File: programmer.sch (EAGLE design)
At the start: 25 parts, among them IC2 74241, U1 ATMEGA8U2, X2 USB-MICROB, Y1 16MHz

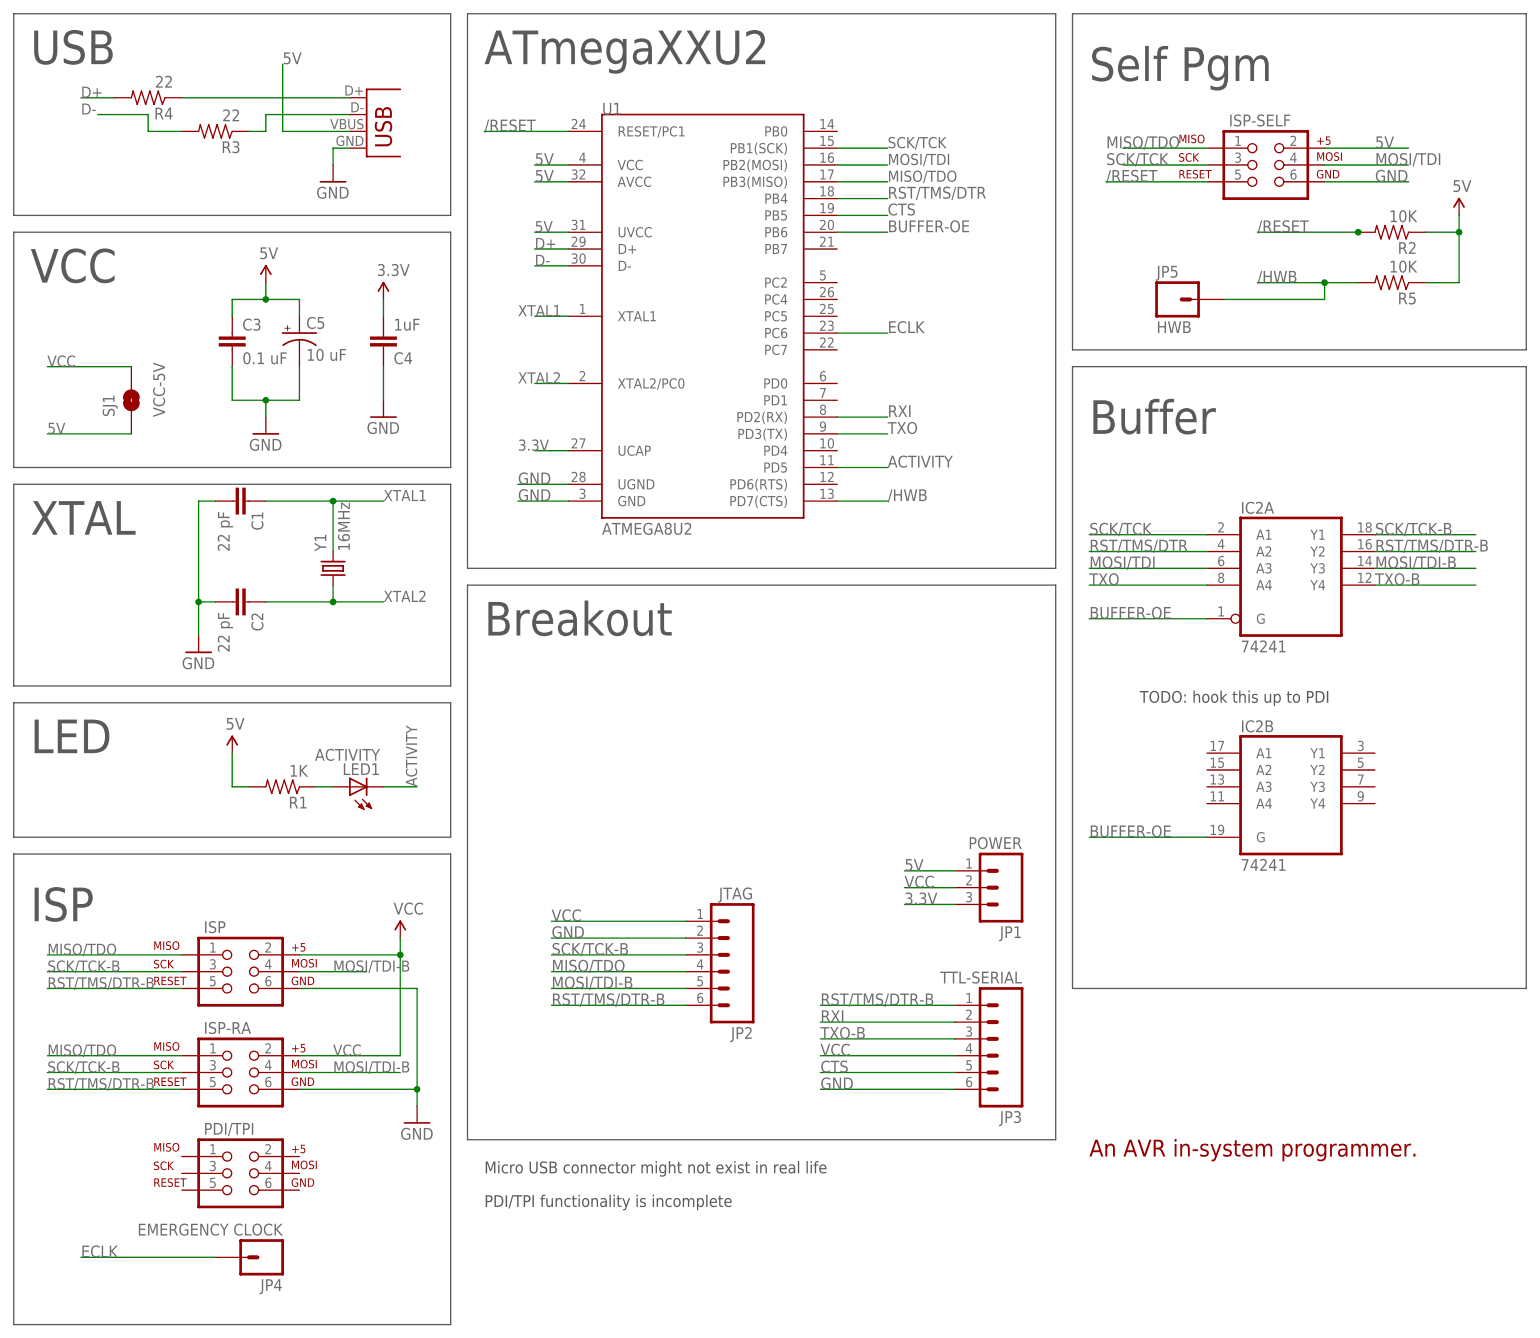
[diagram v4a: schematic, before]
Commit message: Fixed labels. Nothing is obscured.
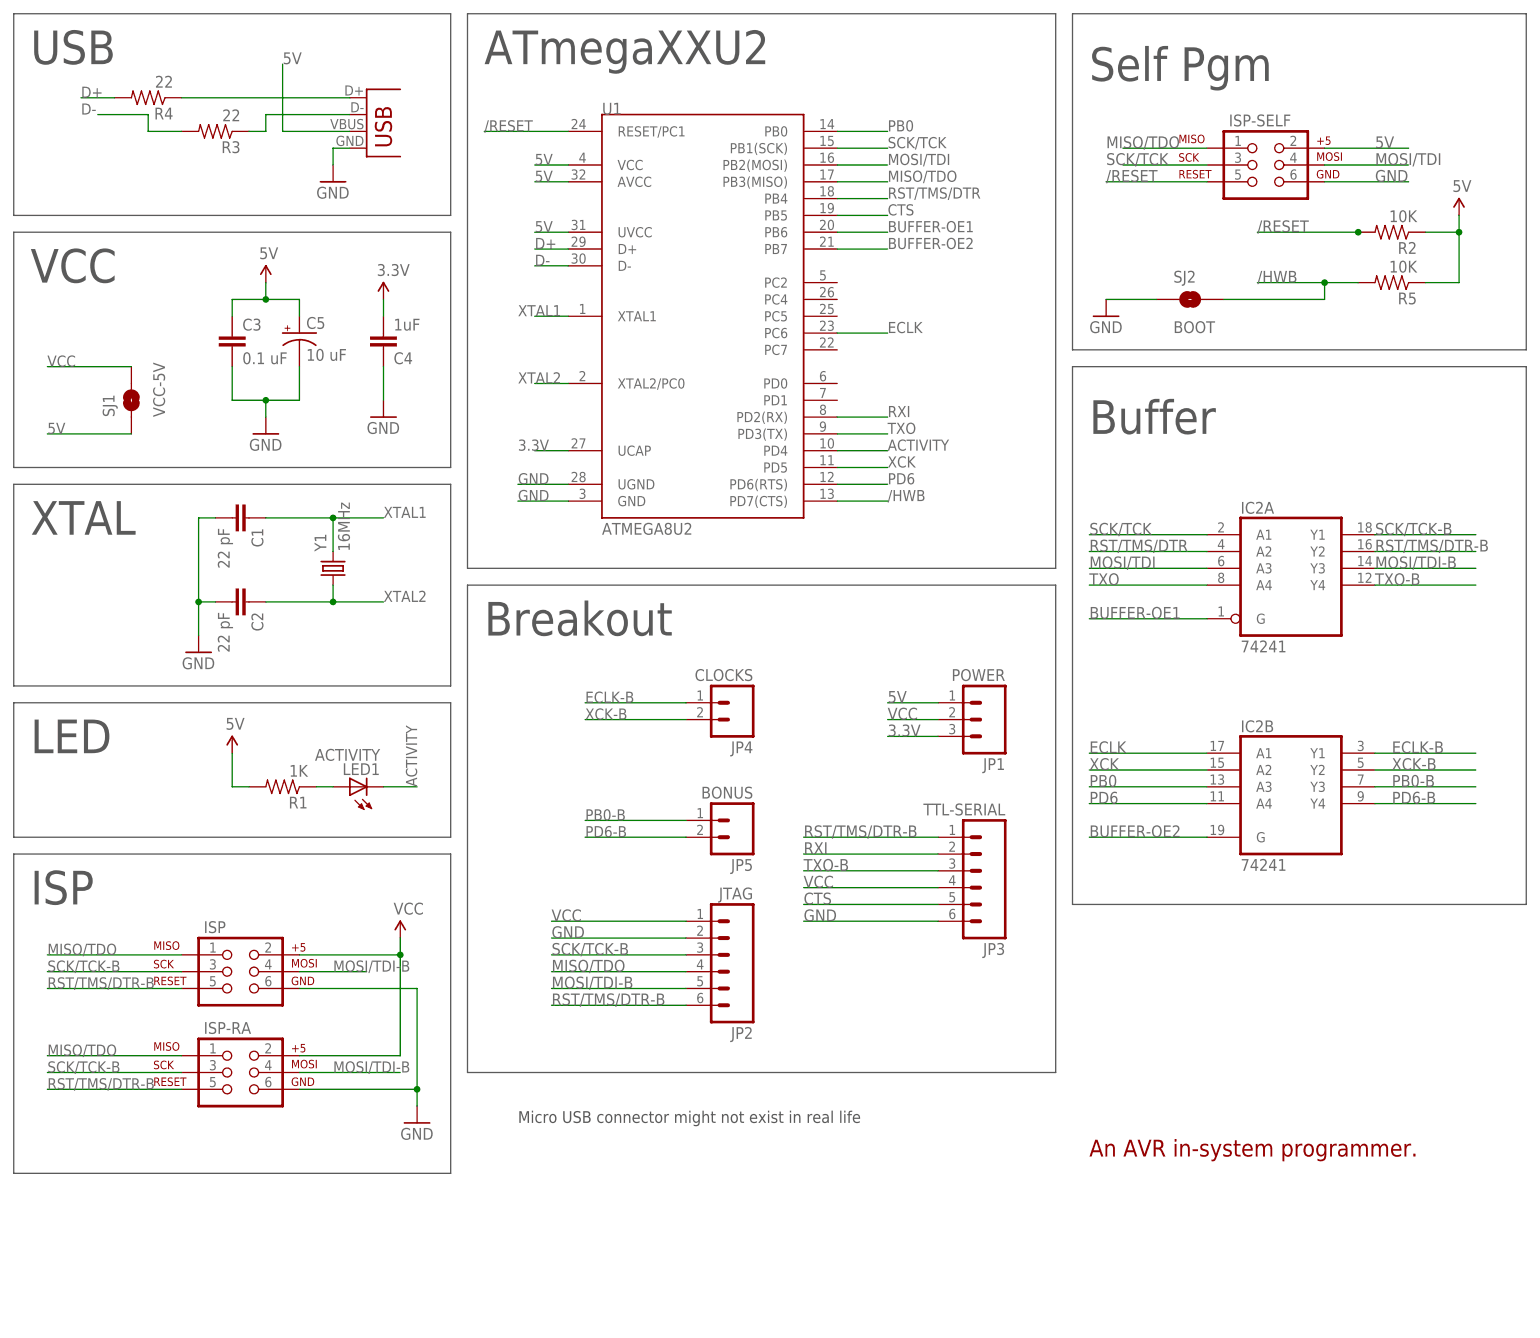
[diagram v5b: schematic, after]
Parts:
- removed PDI/TPI: AVR_SPI_PRG_62X3_LOCK, SparkFun:AVR_SPI_PRG_62X3_LOCK
- added SJ2: BOOT, programmer:SPARKFUN_SOLDERJUMPERNO
- JP4: value EMERGENCY CLOCK -> CLOCKS; device SparkFun:M01PTH -> programmer:M02LOCK
- JP5: value HWB -> BONUS; device SparkFun:M01PTH -> programmer:M02LOCK
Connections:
- removed net BUFFER-OE: IC2A.G, IC2B.G, U1.PB6
- new net BUFFER-OE1: IC2A.G, U1.PB6
- new net BUFFER-OE2: IC2B.G, U1.PB7
- new net ECLK-B: IC2B.Y1, JP4.1
- new net PB0: IC2B.A3, U1.PB0
- new net PB0-B: IC2B.Y3, JP5.1
- new net PD6: IC2B.A4, U1.PD6(RTS)
- new net PD6-B: IC2B.Y4, JP5.2
- new net XCK: IC2B.A2, U1.PD5
- new net XCK-B: IC2B.Y2, JP4.2
- net /HWB: now also SJ2.2; no longer JP5.1
- net ACTIVITY: now also U1.PD4; no longer U1.PD5
- net ECLK: now also IC2B.A1; no longer JP4.1
- net GND: now also SJ2.1
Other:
- note removed: "PDI/TPI functionality is incomplete"
- note removed: "TODO: hook this up to PDI"
- moved on the sheet: C1, JP1, JP3

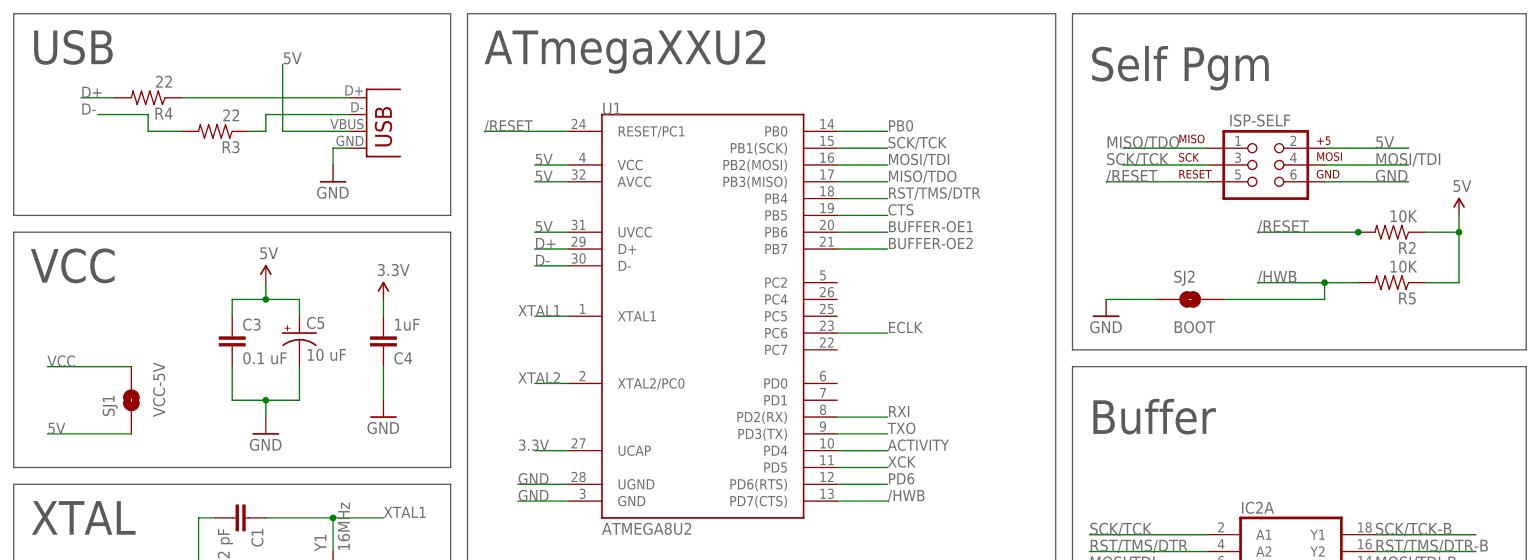
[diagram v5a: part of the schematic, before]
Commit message: Removed unnecessary pullups. Moved bottom labels to right layer.
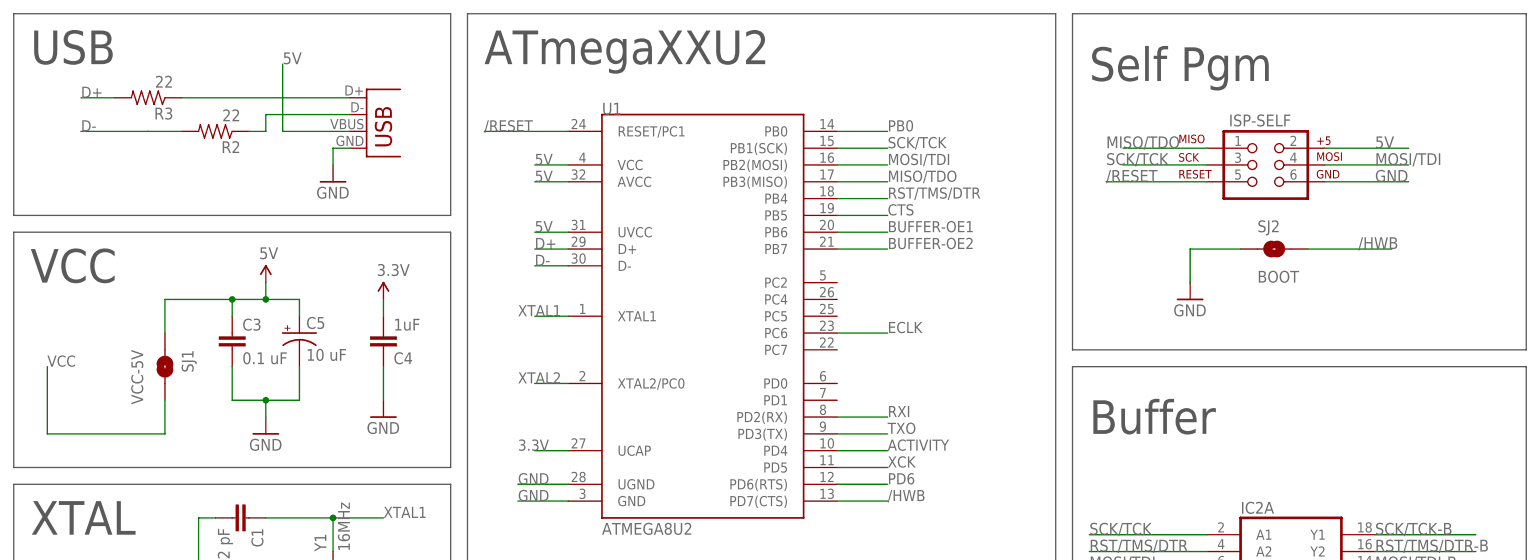
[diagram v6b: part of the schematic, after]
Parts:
- removed R4: 22, SparkFun:RESISTOR0805-RES
- removed R5: 10K, SparkFun:RESISTOR0805-RES
- R2: value 10K -> 22
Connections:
- net /HWB: no longer R5.2
- net /RESET: no longer R2.2
- net 5V: no longer R2.1, R5.1
- net D+: now also R3.2; no longer R4.2
- net D+RAW: now also R3.1; no longer R4.1
- net D-: now also R2.2; no longer R3.2
- net D-RAW: now also R2.1; no longer R3.1
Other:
- moved on the sheet: R2, R3, SJ1, SJ2
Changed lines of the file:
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@@
 <part name="GND5" library="SparkFun" deviceset="GND" device=""/>
 <part name="P+1" library="SparkFun" deviceset="VCC" device=""/>
-<part name="R4" library="SparkFun" deviceset="RESISTOR" device="0805-RES" value="22"/>
 <part name="R3" library="SparkFun" deviceset="RESISTOR" device="0805-RES" value="22"/>
+<part name="R2" library="SparkFun" deviceset="RESISTOR" device="0805-RES" value="22"/>
 <part name="C4" library="SparkFun" deviceset="CAP" device="0805" value="1uF"/>
-<part name="R2" library="SparkFun" deviceset="RESISTOR" device="0805-RES" value="10K"/>
 <part name="P+5" library="SparkFun" deviceset="3.3V" device=""/>
 <part name="FRAME1" library="frames" deviceset="FRAME_A_L" device="" value="SHEET1"/>
@@
 <part name="GND1" library="SparkFun" deviceset="GND" device=""/>
 <part name="U$1" library="SparkFun" deviceset="5V" device=""/>
-<part name="U$2" library="SparkFun" deviceset="5V" device=""/>
 <part name="U$3" library="SparkFun" deviceset="5V" device=""/>
 <part name="ISP" library="SparkFun" deviceset="AVR_SPI_PRG_6" device="2X3_LOCK" value=""/>
@@
 <part name="Y1" library="SparkFun" deviceset="CRYSTAL" device="5X3" value="16MHz"/>
 <part name="JP1" library="SparkFun" deviceset="M03" device="LOCK" value="POWER"/>
-<part name="R5" library="SparkFun" deviceset="RESISTOR" device="0805-RES" value="10K"/>
 <part name="IC2" library="programmer" deviceset="74*241" device=""/>
 <part name="LED1" library="programmer" deviceset="SPARKFUN_LED" device="" value="ACTIVITY"/>
@@
 <instance part="GND5" gate="1" x="0" y="-27.94"/>
 <instance part="P+1" gate="1" x="-2.54" y="0"/>
-<instance part="R4" gate="G$1" x="-40.64" y="127" rot="R180"/>
-<instance part="R3" gate="G$1" x="-30.48" y="121.92" rot="R180"/>
+<instance part="R3" gate="G$1" x="-40.64" y="127" rot="R180"/>
+<instance part="R2" gate="G$1" x="-30.48" y="121.92" rot="R180"/>
 <instance part="C4" gate="G$1" x="-5.08" y="91.44" rot="MR180"/>
-<instance part="R2" gate="G$1" x="147.32" y="106.68" rot="R180"/>
 <instance part="P+5" gate="G$1" x="-5.08" y="96.52"/>
 <instance part="FRAME1" gate="G$1" x="-73.66" y="-63.5"/>
@@
 <instance part="GND1" gate="1" x="-5.08" y="78.74"/>
 <instance part="U$1" gate="G$1" x="-22.86" y="99.06"/>
-<instance part="U$2" gate="G$1" x="157.48" y="109.22"/>
 <instance part="U$3" gate="G$1" x="-27.94" y="27.94"/>
 <instance part="ISP" gate="G$1" x="-27.94" y="-5.08"/>
@@
 <instance part="ISP-SELF" gate="G$1" x="127" y="116.84"/>
 <instance part="X2" gate="G$1" x="-7.62" y="119.38"/>
-<instance part="SJ1" gate="1" x="-43.18" y="81.28" rot="R90"/>
+<instance part="SJ1" gate="1" x="-38.1" y="86.36" rot="R270"/>
 <instance part="JP2" gate="G$1" x="45.72" y="-2.54" rot="R180"/>
 <instance part="JP3" gate="G$1" x="83.82" y="10.16" rot="R180"/>
 <instance part="Y1" gate="G$1" x="-12.7" y="55.88" rot="R90"/>
 <instance part="JP1" gate="G$1" x="86.36" y="33.02" rot="R180"/>
-<instance part="R5" gate="G$1" x="147.32" y="99.06" rot="R180"/>
 <instance part="IC2" gate="A" x="132.08" y="55.88"/>
 <instance part="IC2" gate="B" x="132.08" y="22.86"/>
@@
 <instance part="JP4" gate="G$1" x="48.26" y="35.56" rot="R180"/>
 <instance part="JP5" gate="G$1" x="48.26" y="17.78" rot="R180"/>
-<instance part="SJ2" gate="1" x="116.84" y="96.52"/>
-<instance part="GND4" gate="1" x="104.14" y="93.98"/>
+<instance part="SJ2" gate="1" x="129.54" y="104.14"/>
+<instance part="GND4" gate="1" x="116.84" y="96.52"/>
 </instances>
 <busses>
@@
 <net name="VCC" class="1">
 <segment>
-<wire x1="-55.88" y1="86.36" x2="-43.18" y2="86.36" width="0.1524" layer="91"/>
+<wire x1="-55.88" y1="86.36" x2="-55.88" y2="76.2" width="0.1524" layer="91"/>
+<wire x1="-55.88" y1="76.2" x2="-38.1" y2="76.2" width="0.1524" layer="91"/>
+<wire x1="-38.1" y1="76.2" x2="-38.1" y2="81.28" width="0.1524" layer="91"/>
 <label x="-55.88" y="86.36" size="1.6764" layer="95" font="vector"/>
 <pinref part="SJ1" gate="1" pin="2"/>
@@
 <pinref part="SJ2" gate="1" pin="1"/>
 <pinref part="GND4" gate="1" pin="GND"/>
-<wire x1="111.76" y1="96.52" x2="104.14" y2="96.52" width="0.1524" layer="91"/>
+<wire x1="124.46" y1="104.14" x2="116.84" y2="104.14" width="0.1524" layer="91"/>
+<wire x1="116.84" y1="104.14" x2="116.84" y2="99.06" width="0.1524" layer="91"/>
 </segment>
 </net>
@@
 <segment>
 <wire x1="-10.16" y1="127" x2="-35.56" y2="127" width="0.1524" layer="91"/>
-<pinref part="R4" gate="G$1" pin="1"/>
+<pinref part="R3" gate="G$1" pin="1"/>
 <pinref part="X2" gate="G$1" pin="D+"/>
 </segment>
@@
 <net name="D-RAW" class="0">
 <segment>
-<pinref part="R3" gate="G$1" pin="1"/>
+<pinref part="R2" gate="G$1" pin="1"/>
 <wire x1="-10.16" y1="124.46" x2="-22.86" y2="124.46" width="0.1524" layer="91"/>
 <wire x1="-22.86" y1="124.46" x2="-22.86" y2="121.92" width="0.1524" layer="91"/>
@@
 <net name="D-" class="0">
 <segment>
-<pinref part="R3" gate="G$1" pin="2"/>
+<pinref part="R2" gate="G$1" pin="2"/>
 <wire x1="-35.56" y1="121.92" x2="-40.64" y2="121.92" width="0.1524" layer="91"/>
-<wire x1="-40.64" y1="121.92" x2="-40.64" y2="124.46" width="0.1524" layer="91"/>
-<wire x1="-40.64" y1="124.46" x2="-48.26" y2="124.46" width="0.1524" layer="91"/>
-<label x="-50.8" y="124.46" size="1.6764" layer="95" font="vector"/>
+<wire x1="-40.64" y1="121.92" x2="-50.8" y2="121.92" width="0.1524" layer="91"/>
+<label x="-50.8" y="121.92" size="1.6764" layer="95" font="vector"/>
 </segment>
 <segment>
@@
 <net name="D+" class="0">
 <segment>
-<pinref part="R4" gate="G$1" pin="2"/>
+<pinref part="R3" gate="G$1" pin="2"/>
 <wire x1="-45.72" y1="127" x2="-50.8" y2="127" width="0.1524" layer="91"/>
 <label x="-50.8" y="127" size="1.6764" layer="95" font="vector"/>
@@
 <label x="-20.32" y="132.08" size="1.778" layer="95" font="vector"/>
 <pinref part="X2" gate="G$1" pin="VBUS"/>
-</segment>
-<segment>
-<label x="-55.88" y="76.2" size="1.6764" layer="95" font="vector"/>
-<wire x1="-55.88" y1="76.2" x2="-43.18" y2="76.2" width="0.1524" layer="91"/>
-<pinref part="SJ1" gate="1" pin="1"/>
 </segment>
 <segment>
@@
 <junction x="-22.86" y="96.52"/>
 <pinref part="U$1" gate="G$1" pin="5V"/>
-</segment>
-<segment>
-<pinref part="R2" gate="G$1" pin="1"/>
-<wire x1="152.4" y1="106.68" x2="157.48" y2="106.68" width="0.1524" layer="91"/>
-<pinref part="U$2" gate="G$1" pin="5V"/>
-<wire x1="157.48" y1="106.68" x2="157.48" y2="109.22" width="0.1524" layer="91"/>
-<junction x="157.48" y="106.68"/>
-<wire x1="157.48" y1="106.68" x2="157.48" y2="99.06" width="0.1524" layer="91"/>
-<pinref part="R5" gate="G$1" pin="1"/>
-<wire x1="157.48" y1="99.06" x2="152.4" y2="99.06" width="0.1524" layer="91"/>
+<wire x1="-27.94" y1="96.52" x2="-38.1" y2="96.52" width="0.1524" layer="91"/>
+<wire x1="-38.1" y1="96.52" x2="-38.1" y2="91.44" width="0.1524" layer="91"/>
+<pinref part="SJ1" gate="1" pin="1"/>
+<junction x="-27.94" y="96.52"/>
 </segment>
 <segment>
@@
 <net name="/RESET" class="0">
 <segment>
-<pinref part="R2" gate="G$1" pin="2"/>
-<label x="127" y="106.68" size="1.778" layer="95" font="vector"/>
-<wire x1="142.24" y1="106.68" x2="127" y2="106.68" width="0.1524" layer="91"/>
-<junction x="142.24" y="106.68"/>
-</segment>
-<segment>
 <wire x1="119.38" y1="114.3" x2="104.14" y2="114.3" width="0.1524" layer="91"/>
 <label x="104.14" y="114.3" size="1.778" layer="95" font="vector"/>
@@
 </segment>
 <segment>
-<pinref part="R5" gate="G$1" pin="2"/>
-<wire x1="142.24" y1="99.06" x2="137.16" y2="99.06" width="0.1524" layer="91"/>
-<label x="127" y="99.06" size="1.778" layer="95" font="vector"/>
-<wire x1="137.16" y1="99.06" x2="127" y2="99.06" width="0.1524" layer="91"/>
-<wire x1="121.92" y1="96.52" x2="137.16" y2="96.52" width="0.1524" layer="91"/>
-<wire x1="137.16" y1="96.52" x2="137.16" y2="99.06" width="0.1524" layer="91"/>
-<junction x="137.16" y="99.06"/>
+<label x="142.24" y="104.14" size="1.778" layer="95" font="vector"/>
+<wire x1="134.62" y1="104.14" x2="147.32" y2="104.14" width="0.1524" layer="91"/>
 <pinref part="SJ2" gate="1" pin="2"/>
 </segment>
